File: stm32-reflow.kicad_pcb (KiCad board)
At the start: 4 copper layers, 64 x 59 mm, 59 parts, among them J1 TC2030, J10 63824-1, J11 63824-1, J12 63824-1, J2 Conn_01x04_Male, J3 Conn_01x03_Male, J4 Screw_Terminal_01x02, J5 Screw_Terminal_01x02, J6 Conn_02x08_Odd_Even, J7 63824-1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

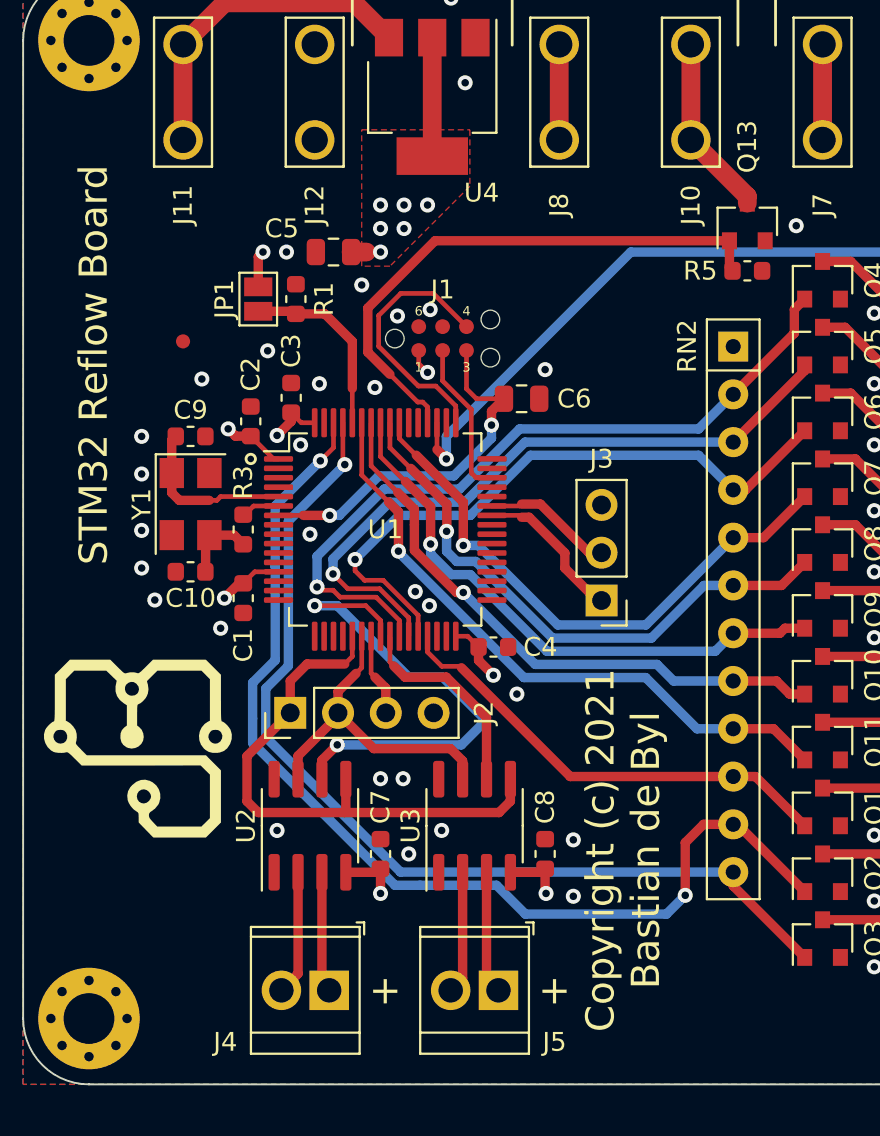
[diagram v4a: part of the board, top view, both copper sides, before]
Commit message: added additional silkscreening
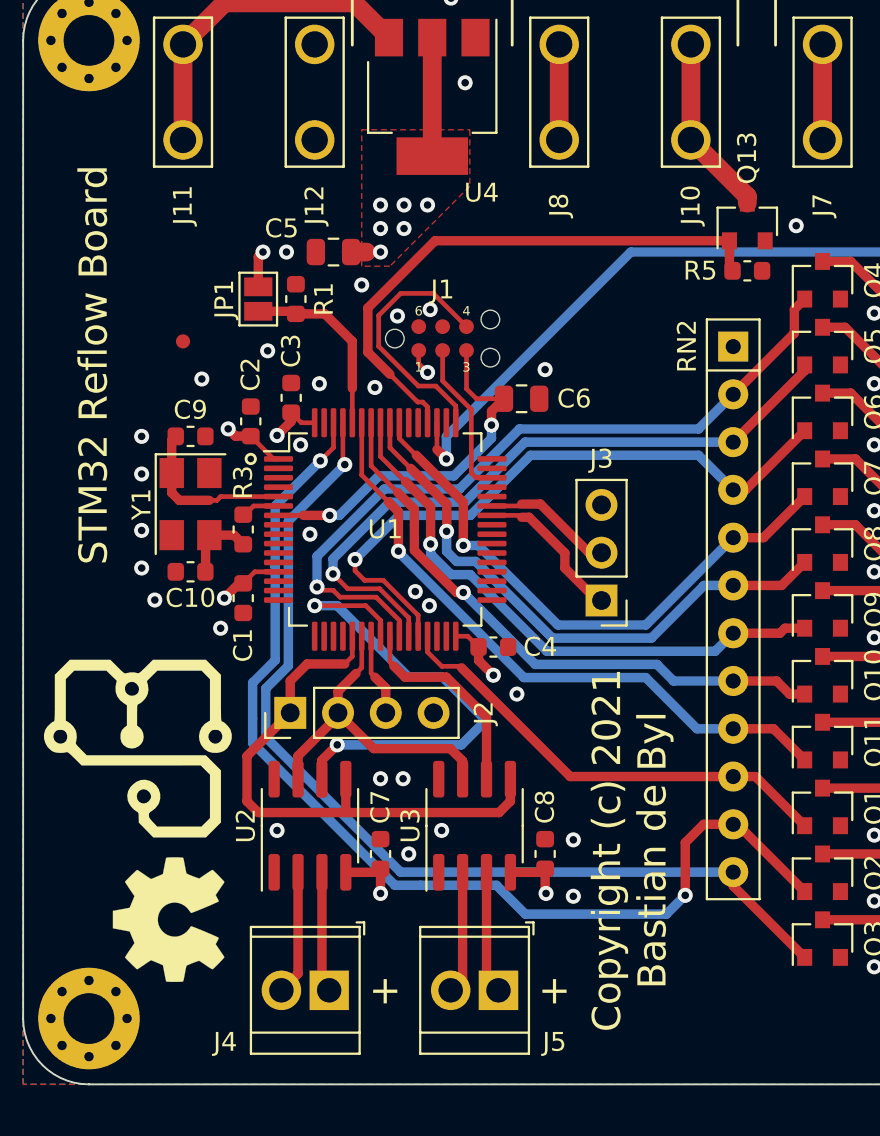
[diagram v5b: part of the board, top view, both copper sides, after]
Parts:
- added REF**: OSHW-Symbol_6.7x6mm_SilkScreen, Symbol:OSHW-Symbol_6.7x6mm_SilkScreen, F.Cu at (119.2, 124.5)
- added REF**: KiCad-Logo2_6mm_SilkScreen, Symbol:KiCad-Logo2_6mm_SilkScreen, B.Cu at (117.6, 118.0)
- added REF**: RoHS-Logo_6mm_SilkScreen, Symbol:RoHS-Logo_6mm_SilkScreen, B.Cu at (144.6, 120.6)
- moved G*** 1.44 mm to (121.4, 92.0), turned to -90 degrees

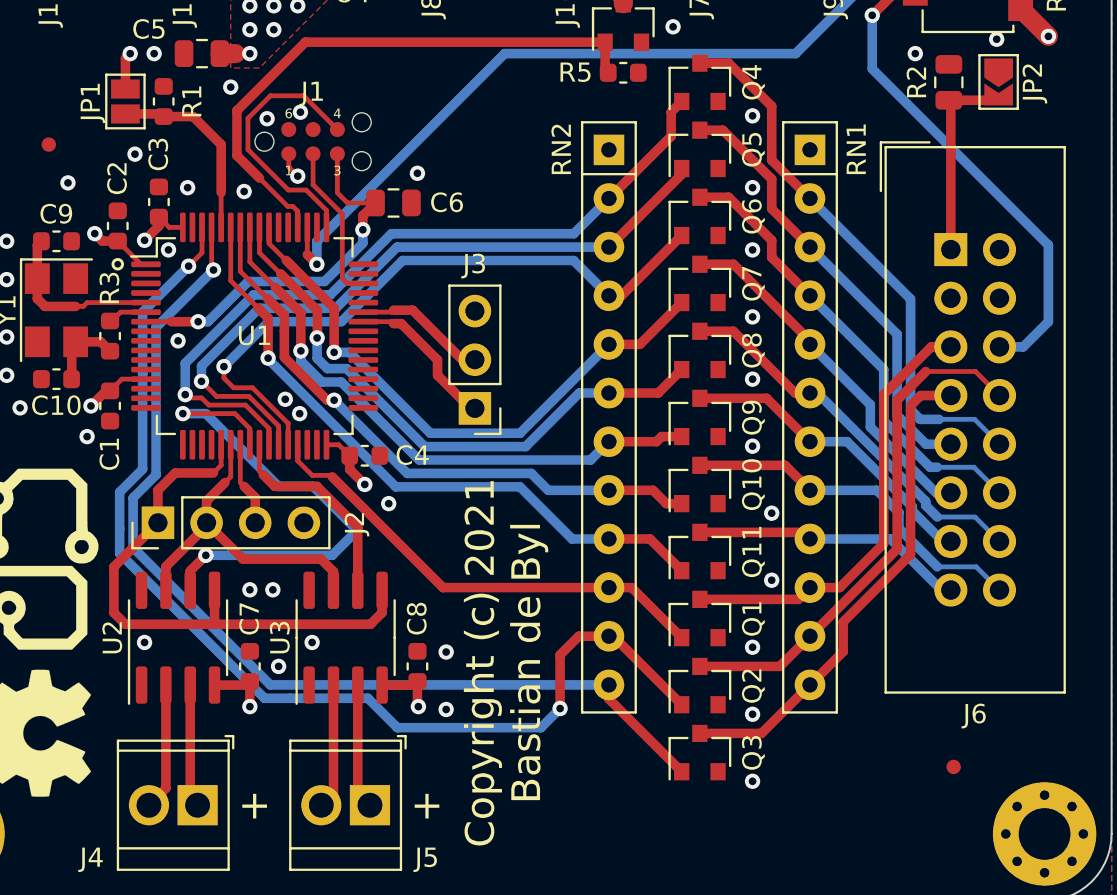
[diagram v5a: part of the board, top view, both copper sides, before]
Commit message: downsized resistor network to 10
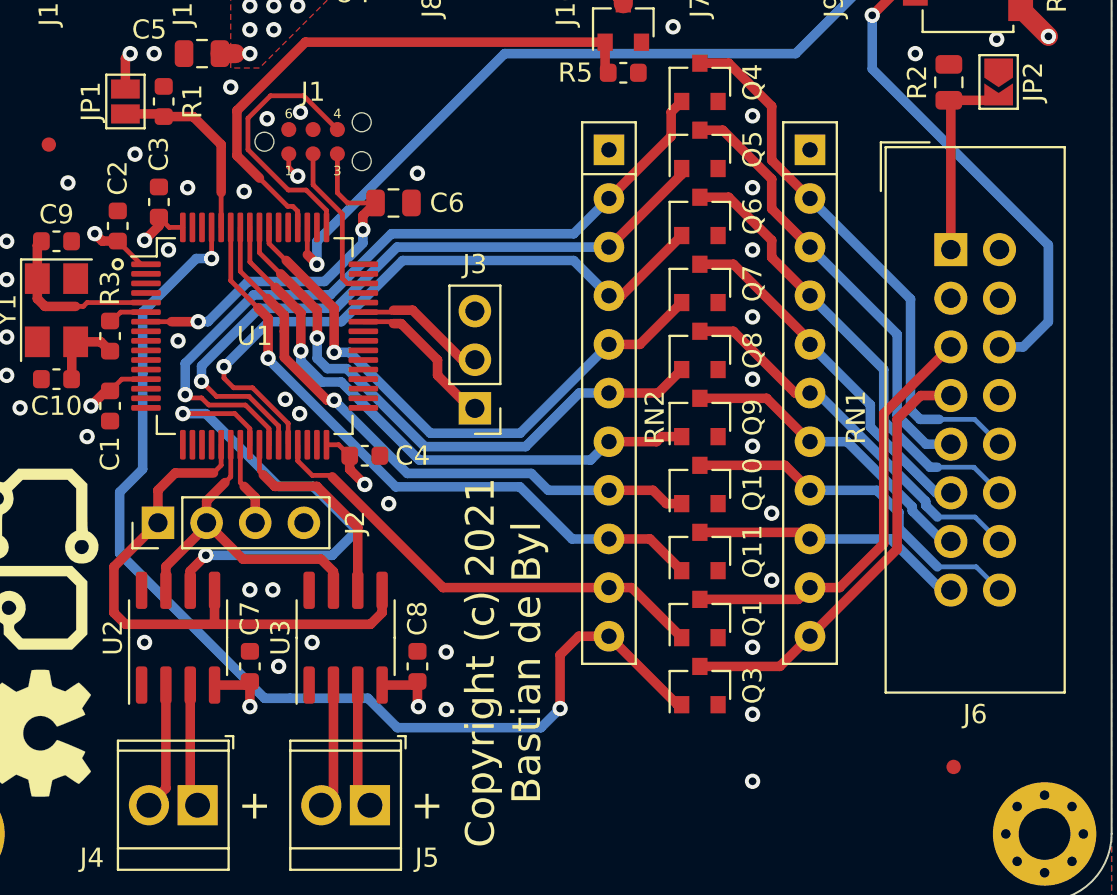
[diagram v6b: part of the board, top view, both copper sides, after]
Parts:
- removed Q2: 2N7002, Package_TO_SOT_SMD:SOT-23
- RN1, RN2: footprint Resistor_THT:R_Array_SIP12 -> Resistor_THT:R_Array_SIP11
- moved Q3 3.50 mm to (154.0, 122.0)
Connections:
- J6 pad 8: /Reflow Level Shifting/LR/~{W} -> GND
- RN1 pad 11: /Reflow Level Shifting/LR/~{W} -> /Reflow Level Shifting/LE
- RN2 pad 11: /Reflow Level Shifting/R/~{W} -> /Reflow Level Shifting/E
- U1 pad 62: /Reflow Level Shifting/R/~{W} -> unconnected-(U1-Pad62)
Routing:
- net /Reflow Level Shifting/R/~{W}: track 57.0 -> 0.00 mm, vias 2 -> 0
- net /Reflow Level Shifting/LR/~{W}: track 27.1 -> 0.00 mm
- net /Reflow Level Shifting/E: track 52.4 -> 57.7 mm, vias 1 -> 2
- net /Reflow Level Shifting/LE: track 25.7 -> 22.9 mm
- net /Reflow Level Shifting/LRS: track 23.1 -> 22.5 mm
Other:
- board text added: "LEDA"

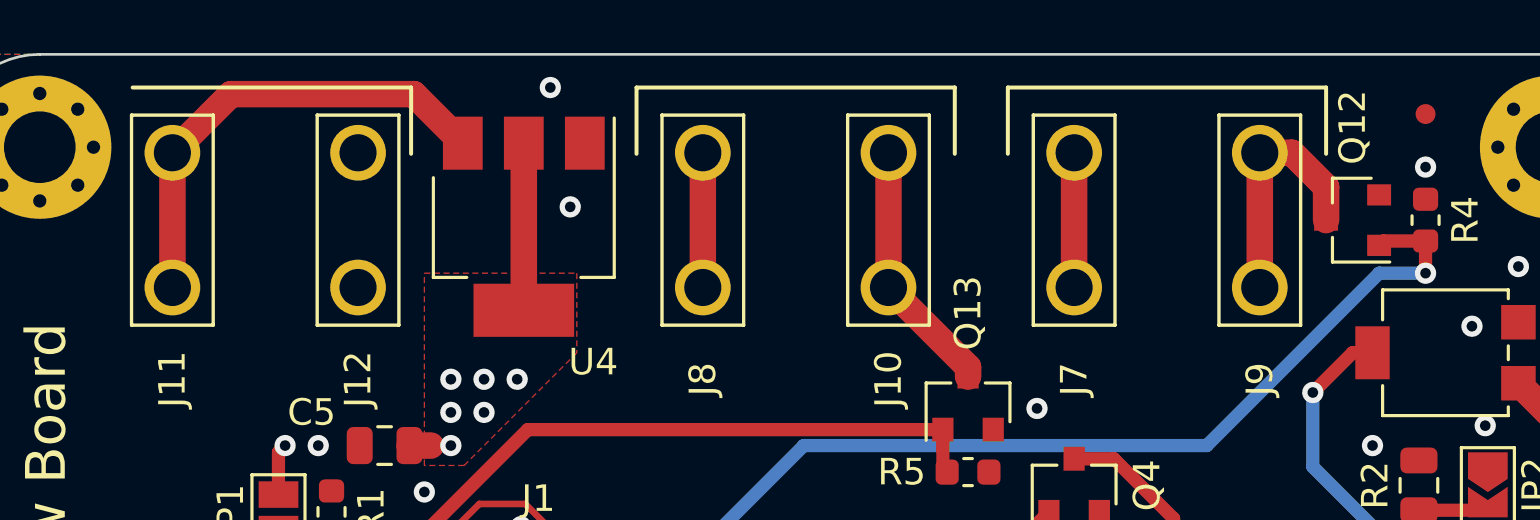
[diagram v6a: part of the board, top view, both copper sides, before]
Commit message: consolidated schematics for clarity, labeling and organization
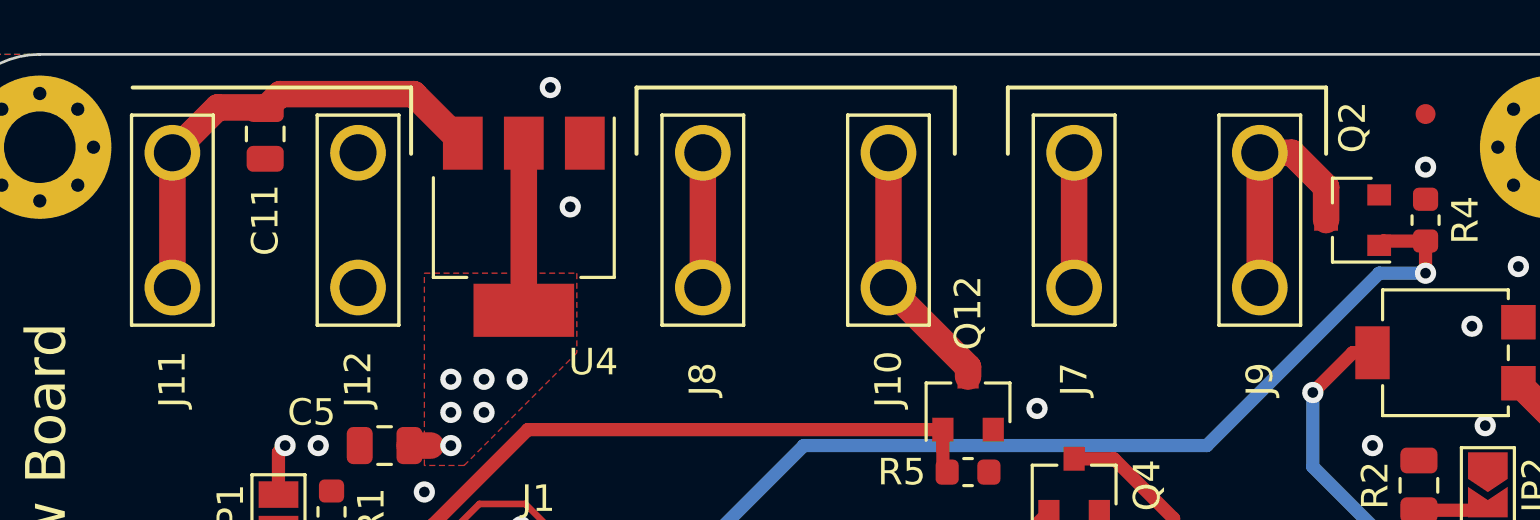
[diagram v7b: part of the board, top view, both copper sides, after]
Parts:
- added C11: 100n, Capacitor_SMD:C_0805_2012Metric, F.Cu at (123.5, 77.2)
- renumbered Q13 to Q12, Q12 to Q2
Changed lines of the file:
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@@
     (property "Comment" "63824-1")
     (property "EU_RoHS_Compliance" "Compliant")
-    (property "Sheetfile" "stm32-reflow-psu.kicad_sch")
-    (property "Sheetname" "Reflow PSU")
+    (property "Sheetfile" "stm32-reflow-mcu.kicad_sch")
+    (property "Sheetname" "Reflow MCU")
     (attr through_hole)
     (fp_text reference "J8" (at 6 0 90) (layer "F.SilkS")
@@
     (property "Comment" "63824-1")
     (property "EU_RoHS_Compliance" "Compliant")
-    (property "Sheetfile" "stm32-reflow-psu.kicad_sch")
-    (property "Sheetname" "Reflow PSU")
+    (property "Sheetfile" "stm32-reflow-mcu.kicad_sch")
+    (property "Sheetname" "Reflow MCU")
     (attr through_hole)
     (fp_text reference "J9" (at 6 0 90) (layer "F.SilkS")
@@
     (property "Comment" "63824-1")
     (property "EU_RoHS_Compliance" "Compliant")
-    (property "Sheetfile" "stm32-reflow-psu.kicad_sch")
-    (property "Sheetname" "Reflow PSU")
+    (property "Sheetfile" "stm32-reflow-mcu.kicad_sch")
+    (property "Sheetname" "Reflow MCU")
     (attr through_hole)
     (fp_text reference "J12" (at 6 0 90) (layer "F.SilkS")
@@
     (descr "Resistor SMD 0603 (1608 Metric), square (rectangular) end terminal, IPC_7351 nominal, (Body size source: http://www.tortai-tech.com/upload/download/2011102023233369053.pdf), generated with kicad-footprint-generator")
     (tags "resistor")
-    (property "Sheetfile" "stm32-reflow-psu.kicad_sch")
-    (property "Sheetname" "Reflow PSU")
+    (property "Sheetfile" "stm32-reflow-mcu.kicad_sch")
+    (property "Sheetname" "Reflow MCU")
     (attr smd)
     (fp_text reference "R5" (at -2.5 0) (layer "F.SilkS")
@@
     (descr "SOT-23, Standard")
     (tags "SOT-23")
-    (property "Sheetfile" "stm32-reflow-psu.kicad_sch")
-    (property "Sheetname" "Reflow PSU")
+    (property "Sheetfile" "stm32-reflow-mcu.kicad_sch")
+    (property "Sheetname" "Reflow MCU")
     (attr smd)
-    (fp_text reference "Q13" (at 3.4 0 90) (layer "F.SilkS")
+    (fp_text reference "Q12" (at 3.4 0 90) (layer "F.SilkS")
       (effects (font (size 1 1) (thickness 0.15)))
     )
@@
     (descr "module CMS SOT223 4 pins")
     (tags "CMS SOT")
-    (property "Sheetfile" "stm32-reflow-psu.kicad_sch")
-    (property "Sheetname" "Reflow PSU")
+    (property "Sheetfile" "stm32-reflow-mcu.kicad_sch")
+    (property "Sheetname" "Reflow MCU")
     (attr smd)
     (fp_text reference "U4" (at 5.102 -2.62) (layer "F.SilkS")
@@
     (property "Comment" "63824-1")
     (property "EU_RoHS_Compliance" "Compliant")
-    (property "Sheetfile" "stm32-reflow-psu.kicad_sch")
-    (property "Sheetname" "Reflow PSU")
+    (property "Sheetfile" "stm32-reflow-mcu.kicad_sch")
+    (property "Sheetname" "Reflow MCU")
     (attr through_hole)
     (fp_text reference "J10" (at 6 0 90) (layer "F.SilkS")
@@
     (property "Comment" "63824-1")
     (property "EU_RoHS_Compliance" "Compliant")
-    (property "Sheetfile" "stm32-reflow-psu.kicad_sch")
-    (property "Sheetname" "Reflow PSU")
+    (property "Sheetfile" "stm32-reflow-mcu.kicad_sch")
+    (property "Sheetname" "Reflow MCU")
     (attr through_hole)
     (fp_text reference "J7" (at 6 0 90) (layer "F.SilkS")
@@
     (descr "Resistor SMD 0603 (1608 Metric), square (rectangular) end terminal, IPC_7351 nominal, (Body size source: http://www.tortai-tech.com/upload/download/2011102023233369053.pdf), generated with kicad-footprint-generator")
     (tags "resistor")
-    (property "Sheetfile" "stm32-reflow-psu.kicad_sch")
-    (property "Sheetname" "Reflow PSU")
+    (property "Sheetfile" "stm32-reflow-mcu.kicad_sch")
+    (property "Sheetname" "Reflow MCU")
     (attr smd)
     (fp_text reference "R4" (at 0 1.5 90) (layer "F.SilkS")
@@
     (property "Comment" "63824-1")
     (property "EU_RoHS_Compliance" "Compliant")
-    (property "Sheetfile" "stm32-reflow-psu.kicad_sch")
-    (property "Sheetname" "Reflow PSU")
+    (property "Sheetfile" "stm32-reflow-mcu.kicad_sch")
+    (property "Sheetname" "Reflow MCU")
     (attr through_hole)
     (fp_text reference "J11" (at 6 0 90) (layer "F.SilkS")
@@
     (descr "SOT-23, Standard")
     (tags "SOT-23")
-    (property "Sheetfile" "stm32-reflow-psu.kicad_sch")
-    (property "Sheetname" "Reflow PSU")
+    (property "Sheetfile" "stm32-reflow-mcu.kicad_sch")
+    (property "Sheetname" "Reflow MCU")
     (attr smd)
-    (fp_text reference "Q12" (at 0 3.5 90) (layer "F.SilkS")
+    (fp_text reference "Q2" (at 0 3.5 90) (layer "F.SilkS")
       (effects (font (size 1 1) (thickness 0.15)))
     )
@@
     )
   )
+  (footprint "Capacitor_SMD:C_0805_2012Metric" (layer "F.Cu")
+    (at 123.5 77.25 -90)
+    (descr "Capacitor SMD 0805 (2012 Metric), square (rectangular) end terminal, IPC_7351 nominal, (Body size source: https://docs.google.com/spreadsheets/d/1BsfQQcO9C6DZCsRaXUlFlo91Tg2WpOkGARC1WS5S8t0/edit?usp=sharing), generated with kicad-footprint-generator")
+    (tags "capacitor")
+    (property "Sheetfile" "stm32-reflow-mcu.kicad_sch")
+    (property "Sheetname" "Reflow MCU")
+    (attr smd)
+    (fp_text reference "C11" (at 3.25 0 90) (layer "F.SilkS")
+      (effects (font (size 1 1) (thickness 0.15)))
+    )
+    (fp_text value "100n" (at 0 1.65 90) (layer "F.Fab")
+      (effects (font (size 1 1) (thickness 0.15)))
+    )
+    (fp_text user "${REFERENCE}" (at 0 0 90) (layer "F.Fab")
+      (effects (font (size 0.5 0.5) (thickness 0.08)))
+    )
+    (fp_line (start -0.258578 -0.71) (end 0.258578 -0.71) (layer "F.SilkS") (width 0.12))
+    (fp_line (start -0.258578 0.71) (end 0.258578 0.71) (layer "F.SilkS") (width 0.12))
+    (fp_line (start 1.68 0.95) (end -1.68 0.95) (layer "F.CrtYd") (width 0.05))
+    (fp_line (start 1.68 -0.95) (end 1.68 0.95) (layer "F.CrtYd") (width 0.05))
+    (fp_line (start -1.68 0.95) (end -1.68 -0.95) (layer "F.CrtYd") (width 0.05))
+    (fp_line (start -1.68 -0.95) (end 1.68 -0.95) (layer "F.CrtYd") (width 0.05))
+    (fp_line (start -1 -0.6) (end 1 -0.6) (layer "F.Fab") (width 0.1))
+    (fp_line (start 1 0.6) (end -1 0.6) (layer "F.Fab") (width 0.1))
+    (fp_line (start 1 -0.6) (end 1 0.6) (layer "F.Fab") (width 0.1))
+    (fp_line (start -1 0.6) (end -1 -0.6) (layer "F.Fab") (width 0.1))
+    (pad "1" smd roundrect locked (at -0.9375 0 270) (size 0.975 1.4) (layers "F.Cu" "F.Paste" "F.Mask") (roundrect_rratio 0.25)
+      (net 16 "+5V") (pintype "passive"))
+    (pad "2" smd roundrect locked (at 0.9375 0 270) (size 0.975 1.4) (layers "F.Cu" "F.Paste" "F.Mask") (roundrect_rratio 0.25)
+      (net 2 "GND") (pintype "passive"))
+    (model "${KISYS3DMOD}/Capacitor_SMD.3dshapes/C_0805_2012Metric.wrl"
+      (offset (xyz 0 0 0))
+      (scale (xyz 1 1 1))
+      (rotate (xyz 0 0 0))
+    )
+  )
   (footprint "Capacitor_SMD:C_0603_1608Metric" (layer "F.Cu")
     (at 136.5 110)
@@
   (segment (start 134.865 121.975) (end 134.865 127.615001) (width 0.5) (layer "F.Cu") (net 15))
   (segment (start 170.75 86.65) (end 172.2 88.1) (width 1) (layer "F.Cu") (net 16))
+  (segment (start 124.0625 75.75) (end 123.5625 76.25) (width 1) (layer "F.Cu") (net 16))
   (segment (start 154 77.96) (end 154 83.04) (width 1) (layer "F.Cu") (net 16))
   (segment (start 140 77.96) (end 140 83.04) (width 1) (layer "F.Cu") (net 16))
-  (segment (start 122.21 75.75) (end 120 77.96) (width 1) (layer "F.Cu") (net 16))
-  (segment (start 129.1 75.75) (end 122.21 75.75) (width 1) (layer "F.Cu") (net 16))
-  (segment (start 120 83.04) (end 120 77.96) (width 1) (layer "F.Cu") (net 16))
+  (segment (start 123.5625 76.25) (end 121.71 76.25) (width 1) (layer "F.Cu") (net 16))
+  (segment (start 129.1 75.75) (end 124.0625 75.75) (width 1) (layer "F.Cu") (net 16))
   (segment (start 130.95 77.6) (end 129.1 75.75) (width 1) (layer "F.Cu") (net 16))
+  (segment (start 120 83.04) (end 120 77.96) (width 1) (layer "F.Cu") (net 16))
+  (segment (start 121.71 76.25) (end 120 77.96) (width 1) (layer "F.Cu") (net 16))
   (via (at 172.2 88.1) (size 0.8) (drill 0.4) (layers "F.Cu" "B.Cu") (net 16))
   (segment (start 167 91.4375) (end 169.367499 91.4375) (width 0.5) (layer "F.Cu") (net 20))
